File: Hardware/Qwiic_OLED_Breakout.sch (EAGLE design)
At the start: 27 parts

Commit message: Post Checklist Changes
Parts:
- added FID3, FID4: FIDUCIAL1X2, SparkFun-Aesthetics:FIDUCIAL1X2
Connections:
- removed net VBAT: C6.1
- net VDD: now also C6.1
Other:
- moved on the sheet: C4, C6
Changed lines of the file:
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@@
 <part name="LOGO2" library="SparkFun-Aesthetics" deviceset="SFE_LOGO_FLAME" device=".1_INCH"/>
 <part name="LOGO4" library="SparkFun-Aesthetics" deviceset="SFE_LOGO_NAME" device=".1_INCH"/>
+<part name="FID3" library="SparkFun-Aesthetics" deviceset="FIDUCIAL" device="1X2"/>
+<part name="FID4" library="SparkFun-Aesthetics" deviceset="FIDUCIAL" device="1X2"/>
 </parts>
 <sheets>
@@
 as long as C3 and C2 are present. It's boosted up from VBAT.</text>
 <text x="179.07" y="146.558" size="1.778" layer="97">3.3 &lt;= VBAT &lt;= 4.2</text>
-<wire x1="147.32" y1="35.56" x2="147.32" y2="121.92" width="0.2032" layer="94"/>
-<wire x1="147.32" y1="121.92" x2="248.92" y2="121.92" width="0.2032" layer="94"/>
-<wire x1="147.32" y1="121.92" x2="147.32" y2="185.42" width="0.2032" layer="94"/>
+<wire x1="147.32" y1="35.56" x2="147.32" y2="121.92" width="0.2032" layer="97" style="shortdash"/>
+<wire x1="147.32" y1="121.92" x2="248.92" y2="121.92" width="0.2032" layer="97" style="shortdash"/>
+<wire x1="147.32" y1="121.92" x2="147.32" y2="185.42" width="0.2032" layer="98" style="shortdash"/>
 <text x="149.86" y="116.84" size="2.54" layer="94">Interface selection</text>
 <text x="106.68" y="129.54" size="1.778" layer="97">D1 (SDAin) and D2 (SDAout)
@@
 <instance part="C2" gate="G$1" x="83.82" y="68.58" rot="MR0"/>
 <instance part="C3" gate="G$1" x="83.82" y="81.28" rot="MR0"/>
-<instance part="C4" gate="G$1" x="119.38" y="162.56"/>
+<instance part="C4" gate="G$1" x="119.38" y="160.02"/>
 <instance part="C5" gate="G$1" x="73.66" y="101.6" rot="MR0"/>
 <instance part="GND2" gate="1" x="78.74" y="93.98"/>
@@
 <instance part="R1" gate="G$1" x="63.5" y="106.68" rot="R90"/>
 <instance part="GND4" gate="1" x="63.5" y="93.98"/>
-<instance part="GND5" gate="1" x="119.38" y="154.94"/>
+<instance part="GND5" gate="1" x="119.38" y="152.4"/>
 <instance part="SUPPLY3" gate="VDD" x="119.38" y="170.18"/>
 <instance part="SUPPLY1" gate="VDD" x="88.9" y="127"/>
 <instance part="FID1" gate="G$1" x="238.76" y="20.32"/>
 <instance part="FID2" gate="G$1" x="238.76" y="17.78"/>
-<instance part="C6" gate="G$1" x="129.54" y="162.56"/>
-<instance part="GND6" gate="1" x="129.54" y="154.94"/>
+<instance part="C6" gate="G$1" x="129.54" y="160.02"/>
+<instance part="GND6" gate="1" x="129.54" y="152.4"/>
 <instance part="LOGO3" gate="G$1" x="12.7" y="10.16"/>
 <instance part="J1" gate="G$1" x="15.24" y="58.42"/>
@@
 <instance part="LOGO2" gate="G$1" x="121.92" y="12.7"/>
 <instance part="LOGO4" gate="G$1" x="88.9" y="0"/>
+<instance part="FID3" gate="G$1" x="241.3" y="20.32"/>
+<instance part="FID4" gate="G$1" x="241.3" y="17.78"/>
 </instances>
 <busses>
@@
 <pinref part="C4" gate="G$1" pin="2"/>
 <pinref part="GND5" gate="1" pin="GND"/>
-<wire x1="119.38" y1="157.48" x2="119.38" y2="160.02" width="0.1524" layer="91"/>
+<wire x1="119.38" y1="154.94" x2="119.38" y2="157.48" width="0.1524" layer="91"/>
 </segment>
 <segment>
 <pinref part="C6" gate="G$1" pin="2"/>
 <pinref part="GND6" gate="1" pin="GND"/>
-<wire x1="129.54" y1="157.48" x2="129.54" y2="160.02" width="0.1524" layer="91"/>
+<wire x1="129.54" y1="154.94" x2="129.54" y2="157.48" width="0.1524" layer="91"/>
 </segment>
 <segment>
@@
 <pinref part="SUPPLY3" gate="VDD" pin="VDD"/>
 <wire x1="119.38" y1="170.18" x2="119.38" y2="167.64" width="0.1524" layer="91"/>
+<pinref part="C6" gate="G$1" pin="1"/>
+<wire x1="119.38" y1="167.64" x2="119.38" y2="165.1" width="0.1524" layer="91"/>
+<wire x1="129.54" y1="165.1" x2="129.54" y2="167.64" width="0.1524" layer="91"/>
+<wire x1="129.54" y1="167.64" x2="119.38" y2="167.64" width="0.1524" layer="91"/>
+<junction x="119.38" y="167.64"/>
 </segment>
 <segment>
@@
 </segment>
 </net>
-<net name="VBAT" class="0">
-<segment>
-<pinref part="C6" gate="G$1" pin="1"/>
-<wire x1="129.54" y1="167.64" x2="129.54" y2="170.18" width="0.1524" layer="91"/>
-<wire x1="129.54" y1="170.18" x2="132.08" y2="170.18" width="0.1524" layer="91"/>
-<label x="132.08" y="170.18" size="1.27" layer="95" xref="yes"/>
-</segment>
-</net>

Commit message: Checklist
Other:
- note added: "v10"
- note removed: "v01"
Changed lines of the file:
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@@
 <sheet>
 <plain>
-<text x="236.982" y="6.35" size="2.54" layer="94" font="vector">v01</text>
+<text x="236.982" y="6.35" size="2.54" layer="94" font="vector">v10</text>
 <text x="178.816" y="150.876" size="1.778" layer="97">1.65 &lt;= VDD &lt;= 3.3</text>
 <text x="195.58" y="129.54" size="1.778" layer="97">VDD current &lt; 300 uA</text>

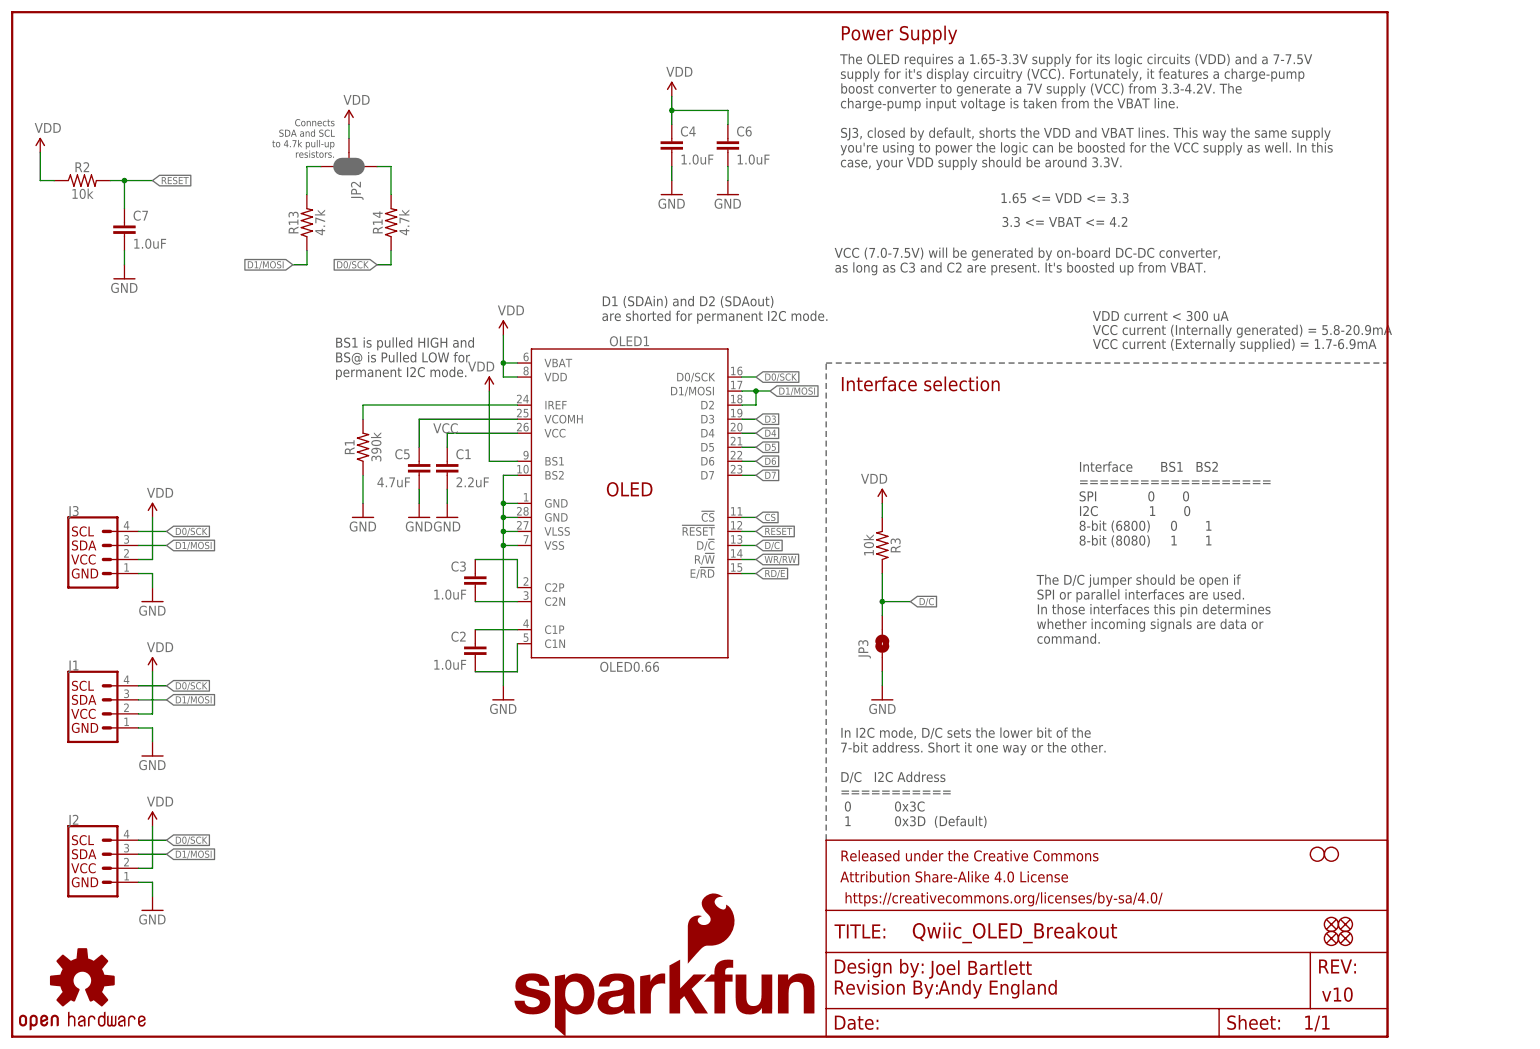
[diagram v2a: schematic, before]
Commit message: Expands the distance between the standoff 0.5" to adhere to our Qwiic standard
* Updates silk
* Organizes schematic
* Adds ordering instructions
* Adds additional measures and units for the measures
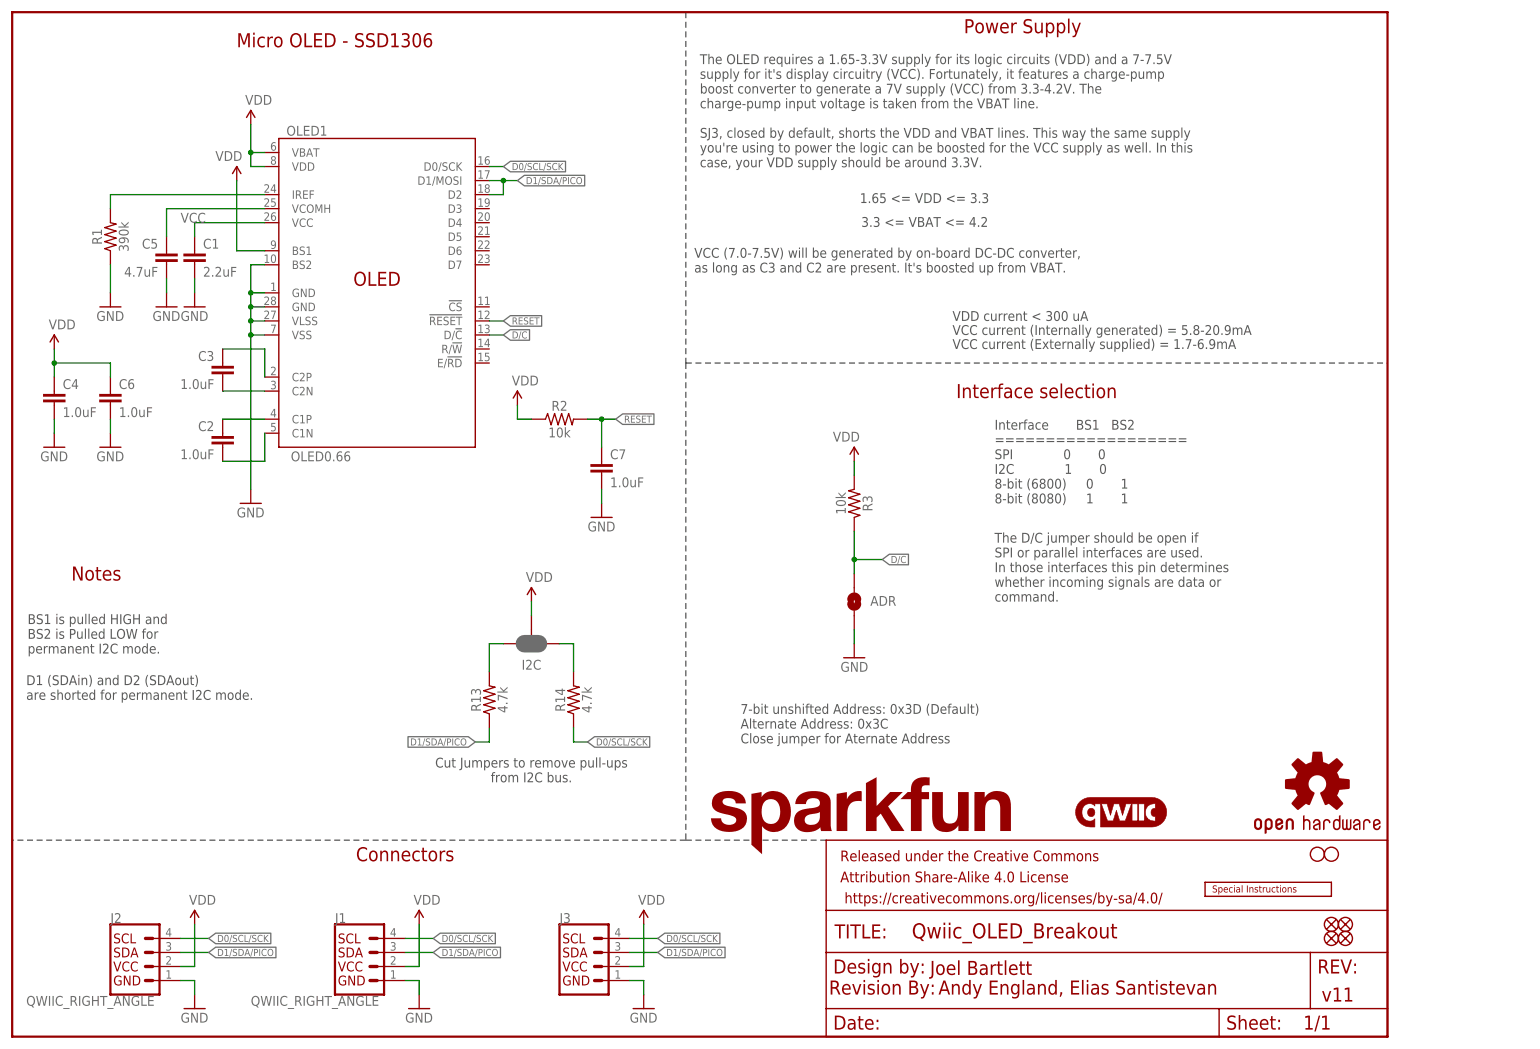
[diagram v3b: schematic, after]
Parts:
- removed JP2: JUMPER-SMT_3_2-NC_PASTE_SILK, SparkFun-Jumpers:JUMPER-SMT_3_2-NC_PASTE_SILK
- removed JP3: JUMPER-SMT_2_NO_SILK, SparkFun-Jumpers:JUMPER-SMT_2_NO_SILK
- removed LOGO4: SFE_LOGO_NAME.1_INCH, SparkFun-Aesthetics:SFE_LOGO_NAME.1_INCH
- added ADR: JUMPER-SMT_2_NO_SILK, SparkFun-Jumpers:JUMPER-SMT_2_NO_SILK
- added I2C: JUMPER-SMT_3_2-NC_PASTE_SILK, SparkFun-Jumpers:JUMPER-SMT_3_2-NC_PASTE_SILK
- added LOGO5: QWIIC_LOGO_4MM, SparkFun-Aesthetics:QWIIC_LOGO_4MM
- added LOGO6: SPECIAL_INSTRUCTIONS-ORDERING, SparkFun-Aesthetics:SPECIAL_INSTRUCTIONS-ORDERING
- J1, J2: value (none) -> QWIIC_RIGHT_ANGLE
- LOGO2: value SFE_LOGO_FLAME.1_INCH -> SFE_LOGO_NAME.1_INCH; device SparkFun-Aesthetics:SFE_LOGO_FLAME.1_INCH -> SparkFun-Aesthetics:SFE_LOGO_NAME.1_INCH
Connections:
- net D0/SCK renamed D0/SCL/SCK
- net D1/MOSI renamed D1/SDA/PICO
- removed net CS: OLED1.!CS!
- removed net D3: OLED1.D3
- removed net D4: OLED1.D4
- removed net D5: OLED1.D5
- removed net D6: OLED1.D6
- removed net D7: OLED1.D7
- removed net RD/E: OLED1.E/!RD!
- removed net WR/RW: OLED1.R/!W!
- net D/C: now also ADR.2; no longer JP3.2
- net GND: now also ADR.1; no longer JP3.1
- net N$4: now also I2C.3; no longer JP2.3
- net N$5: now also I2C.1; no longer JP2.1
- net VDD: now also I2C.2; no longer JP2.2
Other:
- note added: "7-bit unshifted Address: 0x3D (Default) Alternate Address: 0x3C Close jumper for Aternate Address"
- note added: "Andy England, Elias Santistevan"
- note added: "BS1 is pulled HIGH and BS2 is Pulled LOW for permanent I2C mode."
- note added: "Connectors"
- note added: "Cut Jumpers to remove pull-ups from I2C bus."
- note added: "Micro OLED - SSD1306"
- note added: "Notes"
- note added: "v11"
- note removed: "Andy England"
- note removed: "BS1 is pulled HIGH and BS@ is Pulled LOW for permanent I2C mode."
- note removed: "Connects SDA and SCL to 4.7k pull-up resistors."
- note removed: "In I2C mode, D/C sets the lower bit of the 7-bit address. Short it one way or the other. D/C I2C Address =========== 0 0x3C 1 0x3D (Default)"
- note removed: "v10"
- moved on the sheet: C1, C2, C3, C4, C5, C6, C7, J1, J2, J3, OLED1, R1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

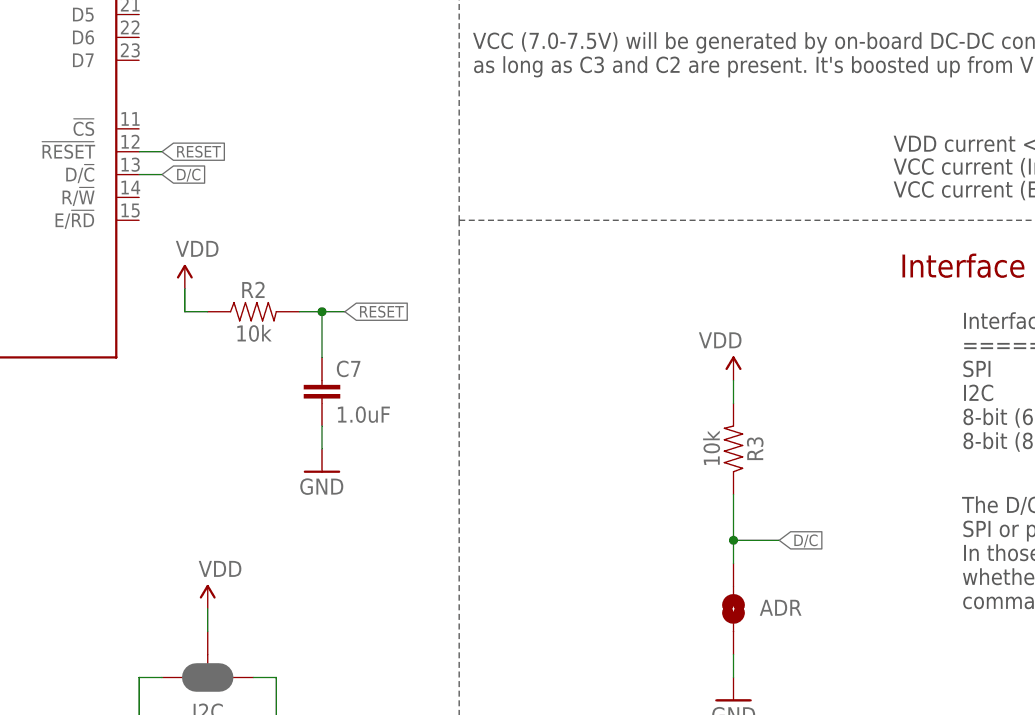
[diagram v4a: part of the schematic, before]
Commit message: Updates D/C net
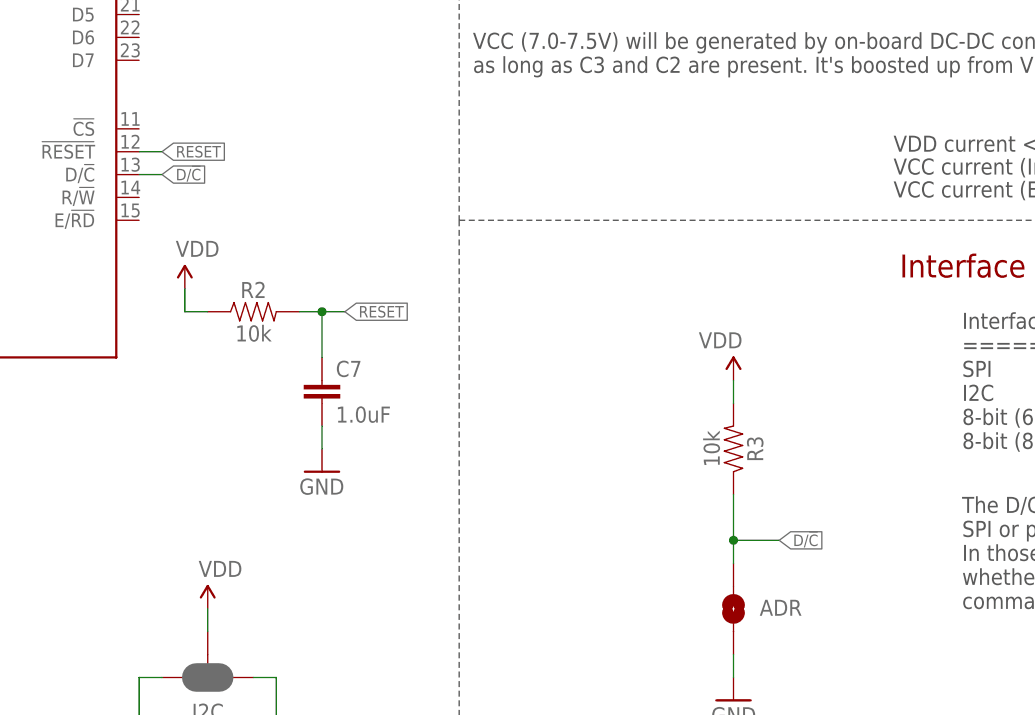
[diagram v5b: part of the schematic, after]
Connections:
- net D/C renamed D/!C!
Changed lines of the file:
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@@
 </segment>
 </net>
-<net name="D/C" class="0">
+<net name="D/!C!" class="0">
 <segment>
 <pinref part="OLED1" gate="G1" pin="D/!C!"/>

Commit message: Fixes mounting hole spacing (derp)
* Adds more measures
* Changes pull up resistor values
* Fixes some notes on ordering instructions
* Adds more notes and silk
* Connects some GND pour
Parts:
- R13, R14: value 4.7k -> 2.2k; device SparkFun-Resistors:4.7KOHM-0603-1/10W-1% -> SparkFun-Resistors:2.2KOHM-0603-1/10W-1%
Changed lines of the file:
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@@
 <part name="GND7" library="SparkFun-Aesthetics" deviceset="GND" device=""/>
 <part name="GND22" library="SparkFun-Aesthetics" deviceset="GND" device=""/>
-<part name="R13" library="SparkFun-Resistors" deviceset="4.7KOHM" device="-0603-1/10W-1%" value="4.7k"/>
-<part name="R14" library="SparkFun-Resistors" deviceset="4.7KOHM" device="-0603-1/10W-1%" value="4.7k"/>
+<part name="R13" library="SparkFun-Resistors" deviceset="2.2KOHM" device="-0603-1/10W-1%" value="2.2k"/>
+<part name="R14" library="SparkFun-Resistors" deviceset="2.2KOHM" device="-0603-1/10W-1%" value="2.2k"/>
 <part name="I2C" library="SparkFun-Jumpers" deviceset="JUMPER-SMT_3_2-NC_PASTE" device="_SILK" package3d_urn="urn:adsk.eagle:package:39294/1" value="JUMPER-SMT_3_2-NC_PASTE_SILK"/>
 <part name="H1" library="SparkFun-Hardware" deviceset="STAND-OFF" device=""/>
